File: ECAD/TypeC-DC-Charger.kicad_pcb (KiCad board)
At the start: 4 copper layers, 48 x 56 mm, 97 parts, among them CON1 XT60-PT-MALE, J1 USB_C_SOCKET_RA_SMD, Q1 CSD18543Q3A, Q2 CSD18543Q3A, Q3 CSD17551Q3A, Q4 CSD17551Q3A, Q5 CSD17579Q3A, Q6 CSD17579Q3A, Q7 CSD17579Q3A, Q8 BC857B, Q9 IRFR9024NTRPBF, SW1 2.54mm_3xSPST_SMD, U1 LM5175RHF, U2 TPS25741, U3 TPS2514

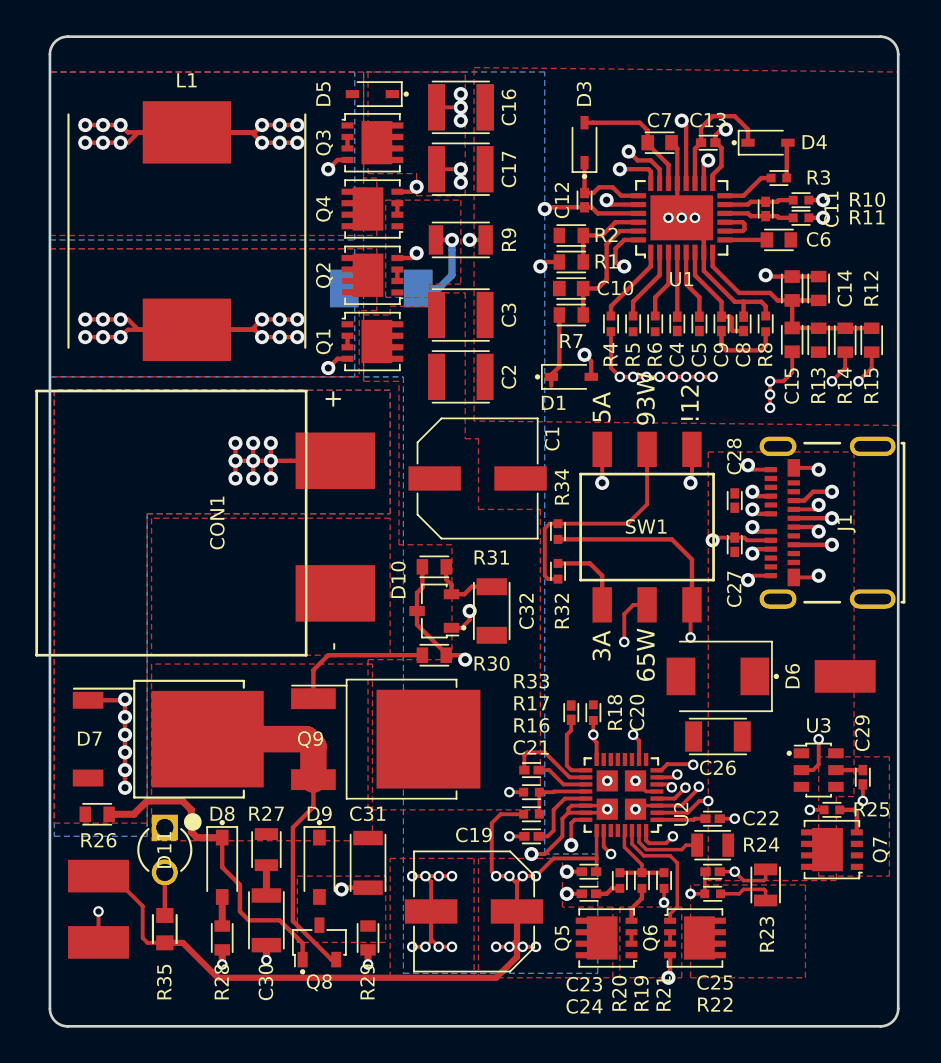
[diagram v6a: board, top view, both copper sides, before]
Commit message: RGB led added. Routing and pours. Removed some DRC errors, fixed cosmetics.
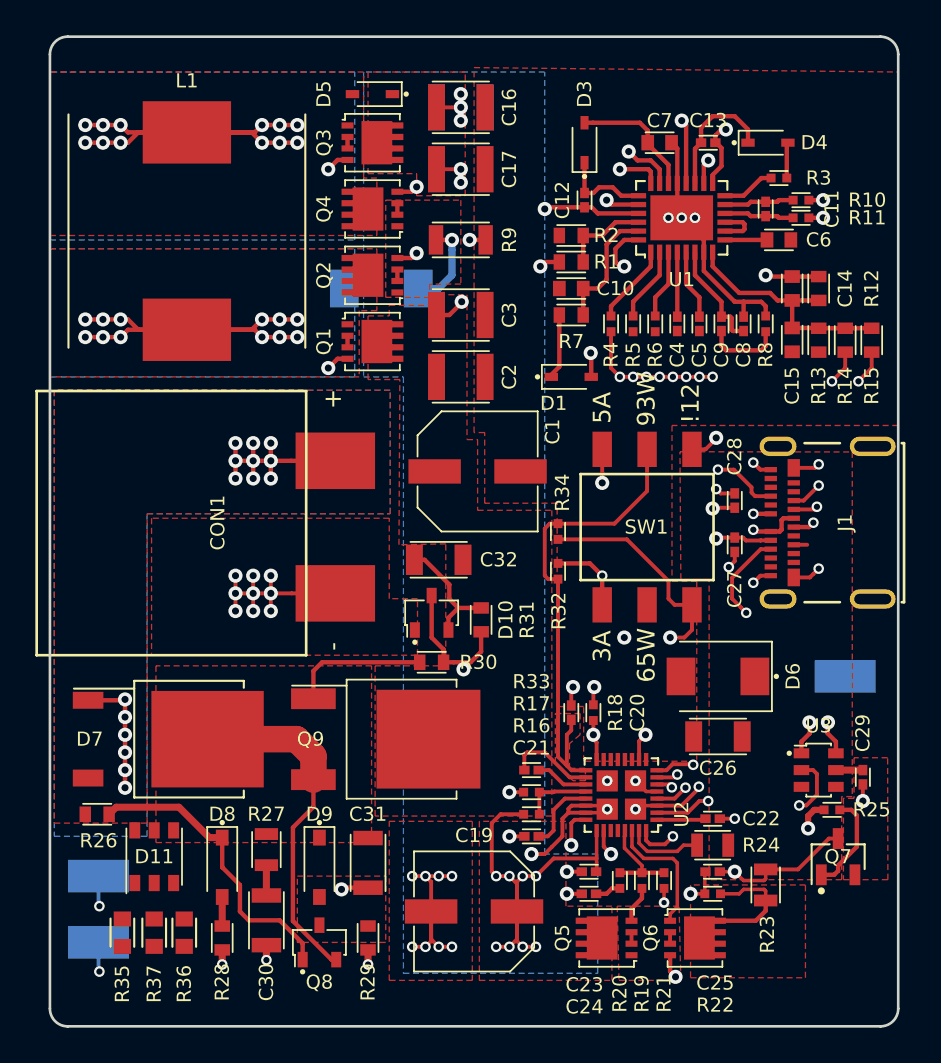
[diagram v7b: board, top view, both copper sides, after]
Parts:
- added R36: 1K00_1608M, Applidyne_Resistor:RESC1608X50N, F.Cu at (107.6, 100.7)
- added R37: 1K00_1608M, Applidyne_Resistor:RESC1608X50N, F.Cu at (105.9, 100.7)
- D11: value LED_RED_3MM_PTH -> LED_RGB_PLCC6; footprint Applidyne_LED:LEDRD254W40D300H700 -> Applidyne_LED:PLCC110P330X340X200-8L
- Q7: value CSD17579Q3A -> 2N7002P; footprint Applidyne_SON:SON65P315X300X90-9T174X245L -> Applidyne_SOT:SOT95P240X110-3L16N
- TEST2, TEST3, TEST5: moved to B.Cu
- moved C32 4.17 mm to (122.0, 79.6), turned to 180 degrees
- moved R31 4.00 mm to (124.4, 83.0), turned to 270 degrees
- moved R35 2.41 mm to (104.1, 100.7)
- moved D11 0.71 mm to (105.9, 96.4), turned to 0 degrees
- moved Q7 0.53 mm to (144.6, 96.4), turned to 0 degrees
- moved R30 0.43 mm to (121.6, 85.4)
- moved C1 0.40 mm to (124.2, 74.6)
- moved D10 0.18 mm to (121.6, 82.6), turned to 0 degrees
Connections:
- R35 pad 1: Net-(D11-PadA) -> Net-(D11-PadC1)
- R35 pad 2: VARIABLE_DC -> CTRL2
- SW1 pad 3: /USBC Controller/PSEL -> (no net)
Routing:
- net CTRL2: track 4.17 -> 34.0 mm
- net CTRL1: track 3.18 -> 32.7 mm
- net VARIABLE_DC: track 76.7 -> 48.3 mm, vias 15 -> 16
- net CC2: track 3.39 -> 29.3 mm, vias 2 -> 3
- net CC1: track 6.60 -> 28.0 mm
- net D-: track 2.66 -> 21.3 mm, vias 2 -> 3
- net /USBC Controller/HIPWR: track 5.35 -> 19.5 mm, vias 1 -> 2
- net D+: track 3.30 -> 17.5 mm
- net VIN: track 10.2 -> 22.7 mm, vias 3 -> 4
- net /USBC Controller/DVDD: track 21.8 -> 32.1 mm
- net GND: track 97.3 -> 107.6 mm, vias 48 -> 57
- net VBUS: track 19.1 -> 28.6 mm, vias 6 -> 5
- net Net-(Q7-Pad1): track 2.15 -> 5.72 mm
- net Net-(Q6-Pad3): track 3.23 -> 6.64 mm
- net /USBC Controller/PSEL: track 11.3 -> 8.51 mm
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- added copper zone on F.Cu, net /USBC Controller/DVDD

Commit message: Updates to schematic and pcb (led and routing)
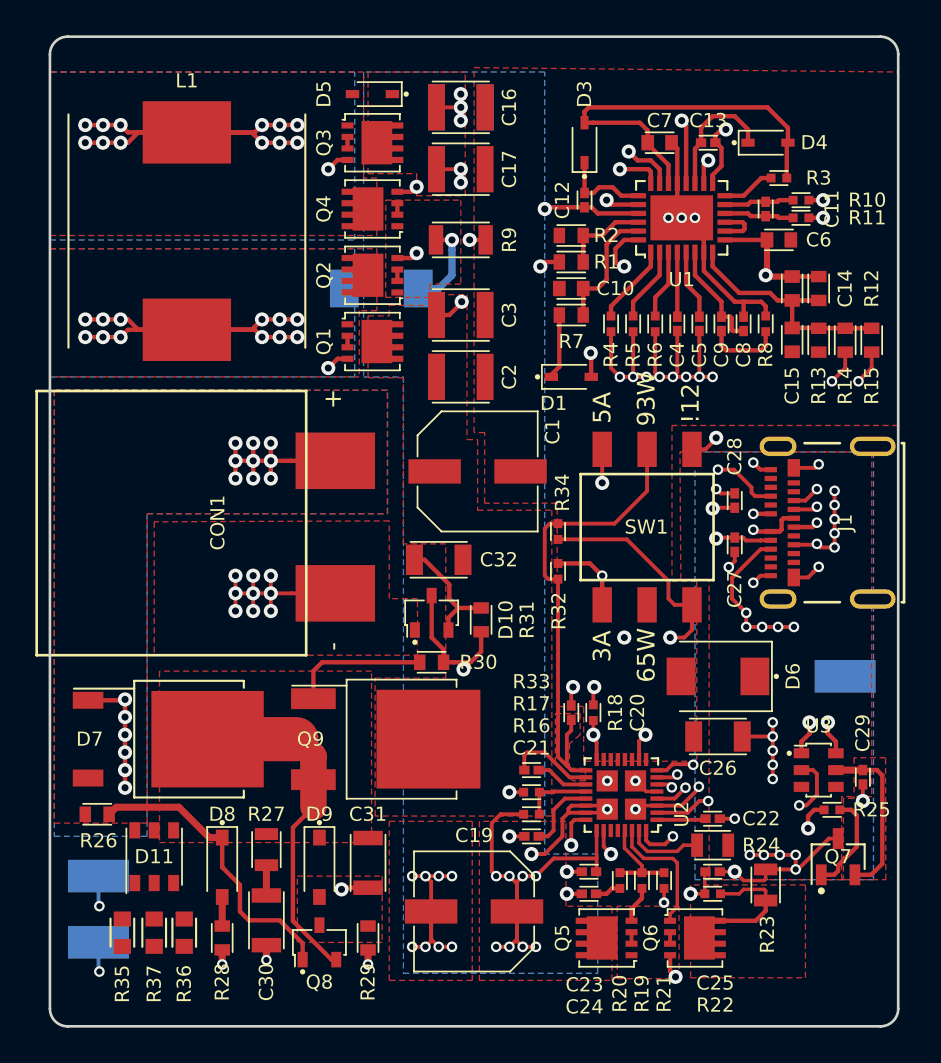
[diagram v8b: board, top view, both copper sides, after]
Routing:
- net VBUS: track 28.6 -> 45.1 mm, vias 5 -> 25
- net /Power Supply/VCC: track 9.26 -> 22.8 mm
- net GND: track 107.6 -> 118.1 mm
- net /Connectors/5V: track 1.53 -> 9.56 mm
- net VARIABLE_DC: track 48.3 -> 50.3 mm
- added copper zone on B.Cu, net VBUS
